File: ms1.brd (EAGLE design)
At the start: 160 x 100 mm, 147 parts, among them IC1 MAX3232EUE, IC2 MAX3380EEUP, J1 POWERPOLE_POWER25A, J10 Radio, J11 A3, J12 A4, J13 A5, J14 A6, J15 A7, J16 D1, J17 D2, J18 D3, J19 D4, J2 ON, J20 D5, J21 D6, J22 D7, J3 LED-EN, J4 RS232, J5 RS485, J6 A1, J7 I2C, J8 A2, J9 TTL_SERIAL, Q1 DMG6602SVT, Q2 DMG6602SVT, Q3 DMG6602SVT, Q4 DMG6602SVT, U1 LT1934ES6TRMPBF, U2 LT1934ES6TRMPBF, U3 DS3231SN, U4 ISL3179EIBZ, X1 KUSBVX-BS1N

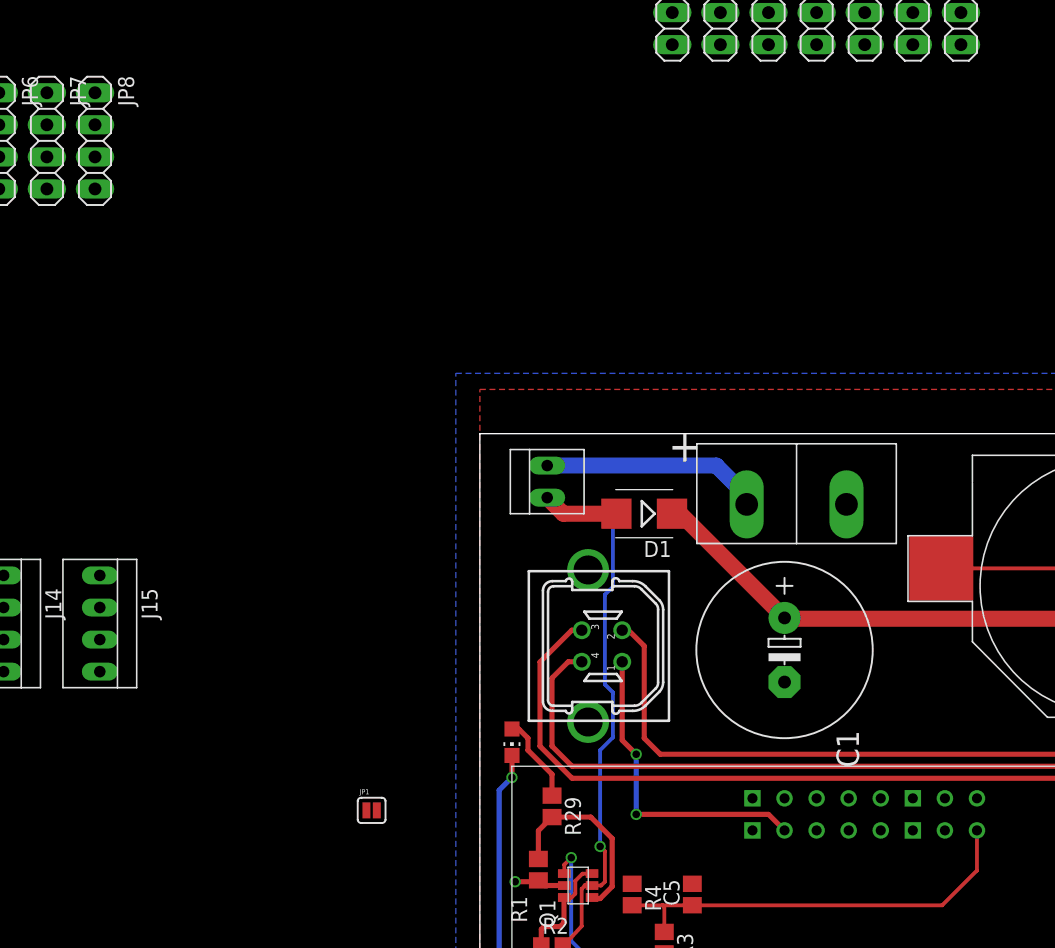
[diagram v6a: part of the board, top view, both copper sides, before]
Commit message: now has cca pin
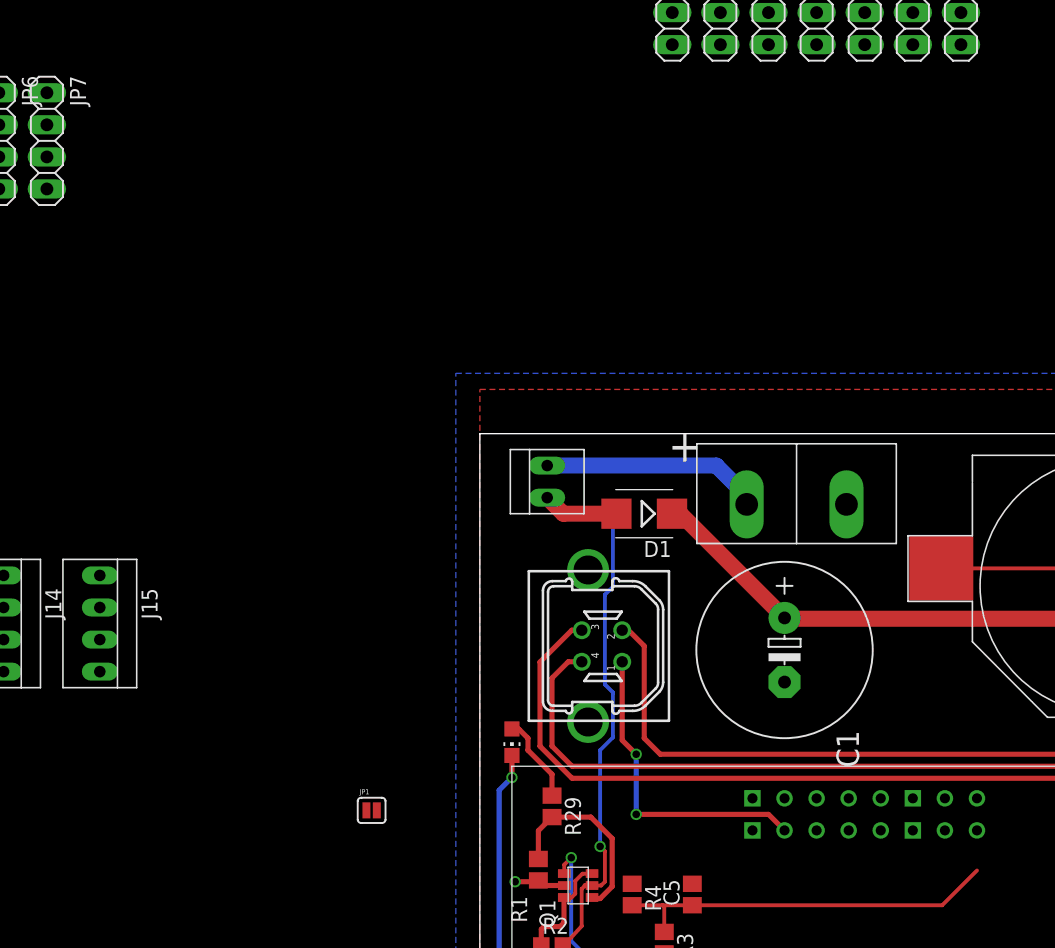
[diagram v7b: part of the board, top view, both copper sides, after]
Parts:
- removed JP8: A7, pinhead:1X04
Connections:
- removed net ADC_0: C5.1, R3.1, R4.2, U$2.A15
- new net RADIO_CCA_STATUS: U$2.C42, U$3.GPIO3
- net ADC_7: now also C5.1, R3.1, R4.2; no longer JP8.3
- net DIO_1: no longer U$2.C42
- net DIO_2: no longer U$2.C51
- net DIO_4: no longer U$2.C50
- net HADC_7: no longer JP8.4
- net SENSE_3V3: no longer JP8.1
- net WADC_7: no longer JP8.2
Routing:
- net ADC_0: track 33.8 -> 0.00 mm
- net ADC_7: track 0.00 -> 30.6 mm
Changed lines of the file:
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@@
 <element name="JP6" library="pinhead" package="1X04" value="A5" x="-38.1" y="123.19" rot="R270"/>
 <element name="JP7" library="pinhead" package="1X04" value="A6" x="-34.29" y="123.19" rot="R270"/>
-<element name="JP8" library="pinhead" package="1X04" value="A7" x="-30.48" y="123.19" rot="R270"/>
 <element name="JP9" library="pinhead" package="1X04" value="D1" x="15.24" y="134.62" rot="R270"/>
 <element name="JP10" library="pinhead" package="1X04" value="D2" x="19.05" y="134.62" rot="R270"/>
@@
 <contactref element="R32" pad="2"/>
 <contactref element="JP2" pad="1"/>
-<contactref element="JP8" pad="1"/>
 <contactref element="JP9" pad="1"/>
 <contactref element="JP7" pad="1"/>
@@
 <wire x1="19.05" y1="138.43" x2="22.86" y2="138.43" width="0" layer="19" extent="1-1"/>
 <wire x1="15.24" y1="138.43" x2="19.05" y2="138.43" width="0" layer="19" extent="1-1"/>
-<wire x1="-30.48" y1="127" x2="15.24" y2="138.43" width="0" layer="19" extent="1-1"/>
-<wire x1="-34.29" y1="127" x2="-30.48" y2="127" width="0" layer="19" extent="1-1"/>
+<wire x1="-34.29" y1="127" x2="15.24" y2="138.43" width="0" layer="19" extent="1-1"/>
 <wire x1="-38.1" y1="127" x2="-34.29" y2="127" width="0" layer="19" extent="1-1"/>
 <wire x1="-41.91" y1="127" x2="-38.1" y2="127" width="0" layer="19" extent="1-1"/>
@@
 <wire x1="103.4215" y1="93.2615" x2="100.8815" y2="93.2615" width="0.6096" layer="1"/>
 </signal>
-<signal name="ADC_0">
-<contactref element="R4" pad="2"/>
-<contactref element="R3" pad="1"/>
-<contactref element="C5" pad="1"/>
-<contactref element="U$2" pad="A15"/>
-<wire x1="12.065" y1="62.65" x2="14.478" y2="62.65" width="0.3048" layer="1"/>
-<wire x1="14.478" y1="62.65" x2="16.8275" y2="62.65" width="0.3048" layer="1"/>
-<wire x1="14.605" y1="60.54" x2="14.605" y2="62.523" width="0.3048" layer="1"/>
-<wire x1="14.605" y1="62.523" x2="14.478" y2="62.65" width="0.3048" layer="1"/>
-<wire x1="16.8275" y1="62.65" x2="36.615" y2="62.65" width="0.3048" layer="1"/>
-<wire x1="36.615" y1="62.65" x2="39.37" y2="65.405" width="0.3048" layer="1"/>
-<wire x1="39.37" y1="65.405" x2="39.37" y2="68.58" width="0.3048" layer="1"/>
-</signal>
 <signal name="VCC_HP2_SW1">
 <contactref element="R3" pad="2"/>
@@
 <signal name="DIO_4">
 <contactref element="R15" pad="2"/>
-<contactref element="U$2" pad="C50"/>
 <contactref element="JP12" pad="3"/>
-<wire x1="29.21" y1="40.64" x2="26.67" y2="133.35" width="0" layer="19" extent="1-1"/>
 <wire x1="-189.23" y1="133.77" x2="26.67" y2="133.35" width="0" layer="19" extent="1-1"/>
 </signal>
@@
 <signal name="DIO_2">
 <contactref element="R10" pad="2"/>
-<contactref element="U$2" pad="C51"/>
 <contactref element="JP10" pad="3"/>
-<wire x1="26.67" y1="43.18" x2="19.05" y2="133.35" width="0" layer="19" extent="1-1"/>
 <wire x1="-201.93" y1="133.77" x2="19.05" y2="133.35" width="0" layer="19" extent="1-1"/>
 </signal>
@@
 <signal name="DIO_1">
 <contactref element="R8" pad="2"/>
-<contactref element="U$2" pad="C42"/>
 <contactref element="JP9" pad="3"/>
-<wire x1="39.37" y1="40.64" x2="15.24" y2="133.35" width="0" layer="19" extent="1-1"/>
 <wire x1="-209.55" y1="133.77" x2="15.24" y2="133.35" width="0" layer="19" extent="1-1"/>
 </signal>
@@
 <signal name="ADC_7">
 <contactref element="U$2" pad="A6"/>
-<contactref element="JP8" pad="3"/>
-<wire x1="-30.48" y1="121.92" x2="26.67" y2="71.12" width="0" layer="19" extent="1-1"/>
+<contactref element="R4" pad="2"/>
+<contactref element="R3" pad="1"/>
+<contactref element="C5" pad="1"/>
+<wire x1="12.065" y1="62.65" x2="14.478" y2="62.65" width="0.3048" layer="1"/>
+<wire x1="14.478" y1="62.65" x2="16.8275" y2="62.65" width="0.3048" layer="1"/>
+<wire x1="14.605" y1="60.54" x2="14.605" y2="62.523" width="0.3048" layer="1"/>
+<wire x1="14.605" y1="62.523" x2="14.478" y2="62.65" width="0.3048" layer="1"/>
+<wire x1="16.8275" y1="62.65" x2="36.615" y2="62.65" width="0.3048" layer="1"/>
+<wire x1="36.615" y1="62.65" x2="39.37" y2="65.405" width="0.3048" layer="1"/>
+<wire x1="16.8275" y1="62.65" x2="26.67" y2="71.12" width="0" layer="19" extent="1-1"/>
 </signal>
 <signal name="WADC_4">
@@
 <signal name="WADC_7">
 <contactref element="U$4" pad="S14"/>
-<contactref element="JP8" pad="2"/>
-<wire x1="-30.48" y1="124.46" x2="127.381" y2="5.588" width="0" layer="19" extent="1-1"/>
 </signal>
 <signal name="BZ">
@@
 </signal>
 <signal name="HADC_7">
-<contactref element="JP8" pad="4"/>
 <contactref element="J15" pad="2"/>
-<wire x1="-30.099" y1="83.693" x2="-30.48" y2="119.38" width="0" layer="19" extent="1-1"/>
 </signal>
 <signal name="HDIO_1">
@@
 <wire x1="36.918" y1="9.818" x2="37.719" y2="9.818" width="0.4064" layer="1"/>
 </signal>
+<signal name="RADIO_CCA_STATUS">
+<contactref element="U$3" pad="GPIO3"/>
+<contactref element="U$2" pad="C42"/>
+<wire x1="45.974" y1="6.985" x2="39.37" y2="40.64" width="0" layer="19" extent="1-1"/>
+</signal>
 </signals>

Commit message: routed GPIO3
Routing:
- net RADIO_CCA_STATUS: track 0.00 -> 44.1 mm, vias 0 -> 1
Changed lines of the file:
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@@
 <contactref element="U$3" pad="GPIO3"/>
 <contactref element="U$2" pad="C42"/>
-<wire x1="45.974" y1="6.985" x2="39.37" y2="40.64" width="0" layer="19" extent="1-1"/>
+<wire x1="45.974" y1="6.985" x2="47.879" y2="6.985" width="0.4064" layer="1"/>
+<wire x1="47.879" y1="6.985" x2="48.133" y2="7.239" width="0.4064" layer="1"/>
+<wire x1="48.133" y1="7.239" x2="48.133" y2="19.558" width="0.4064" layer="1"/>
+<wire x1="48.133" y1="19.558" x2="46.736" y2="20.955" width="0.4064" layer="1"/>
+<wire x1="46.736" y1="20.955" x2="45.085" y2="20.955" width="0.4064" layer="1"/>
+<wire x1="45.085" y1="20.955" x2="43.815" y2="22.225" width="0.4064" layer="1"/>
+<via x="43.815" y="22.225" extent="1-16" drill="0.4826"/>
+<wire x1="43.815" y1="22.225" x2="43.815" y2="41.021" width="0.4064" layer="16"/>
+<wire x1="43.815" y1="41.021" x2="42.926" y2="41.91" width="0.4064" layer="16"/>
+<wire x1="42.926" y1="41.91" x2="40.64" y2="41.91" width="0.4064" layer="16"/>
+<wire x1="40.64" y1="41.91" x2="39.37" y2="40.64" width="0.4064" layer="16"/>
 </signal>
 </signals>
